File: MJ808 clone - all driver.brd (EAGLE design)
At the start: 22 x 22 mm, 35 parts, among them IC1 ATTINY4313-MMH, IC2 PRQV8.00CR1510Y00L, IC3 LP38693SD-5.0/NOPB, IC4 LP38693SD-5.0/NOPB, IC5 MCP2515, IC6 MCP2561-2, IC7 MAX16820, Q1 PMV213SN,215, SW1 TL3305-844809

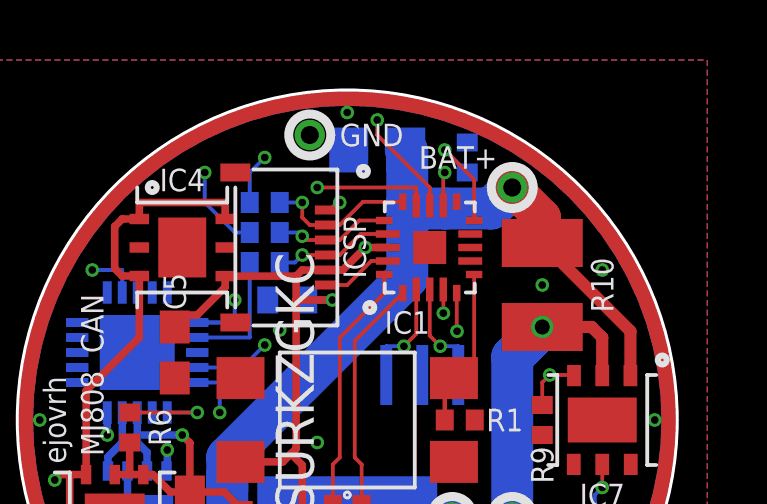
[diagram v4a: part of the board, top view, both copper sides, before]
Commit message: - rerouted standby pin, updated gerbers
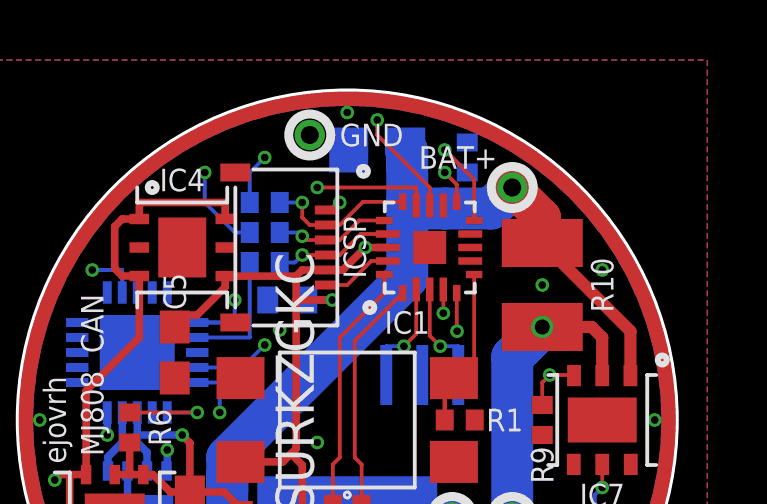
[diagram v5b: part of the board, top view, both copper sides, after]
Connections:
- net N$3: now also IC1.PB2; no longer IC1.PB1
- net STBY: now also IC1.PB1; no longer IC1.PB2
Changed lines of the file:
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@@
 <layers>
 <layer number="1" name="Top" color="4" fill="1" visible="yes" active="yes"/>
-<layer number="2" name="Route2" color="1" fill="3" visible="yes" active="yes"/>
+<layer number="2" name="Route2" color="1" fill="3" visible="no" active="yes"/>
 <layer number="3" name="Route3" color="4" fill="3" visible="no" active="no"/>
 <layer number="4" name="Route4" color="1" fill="4" visible="no" active="no"/>
@@
 <layer number="13" name="Route13" color="4" fill="5" visible="no" active="no"/>
 <layer number="14" name="Route14" color="1" fill="6" visible="no" active="no"/>
-<layer number="15" name="Route15" color="4" fill="6" visible="yes" active="yes"/>
+<layer number="15" name="Route15" color="4" fill="6" visible="no" active="yes"/>
 <layer number="16" name="Bottom" color="1" fill="1" visible="yes" active="yes"/>
 <layer number="17" name="Pads" color="2" fill="1" visible="yes" active="yes"/>
@@
 <contactref element="IC6" pad="STBY"/>
 <contactref element="R11" pad="2"/>
-<contactref element="IC1" pad="PB2"/>
 <via x="3.25" y="8.25" extent="1-16" drill="0.254"/>
-<wire x1="3.25" y1="8.25" x2="3.25" y2="4.5" width="0.254" layer="15"/>
-<wire x1="3.25" y1="4.5" x2="-5.290875" y2="-4.040875" width="0.254" layer="15"/>
+<wire x1="3.25" y1="8.25" x2="3.25" y2="5.25" width="0.254" layer="15"/>
 <wire x1="-7.975" y1="-4.8" x2="-7.975" y2="-5.975" width="0.127" layer="16"/>
 <via x="-7.375" y="-6.875" extent="1-16" drill="0.254"/>
@@
 <wire x1="-7.975" y1="-4.8" x2="-7.975" y2="-6.275" width="0.127" layer="16"/>
 <wire x1="-7.975" y1="-6.275" x2="-7.375" y2="-6.875" width="0.127" layer="16"/>
-<wire x1="-5.290875" y1="-5.25" x2="-5.290875" y2="-4.040875" width="0.254" layer="15"/>
+<wire x1="-5.290875" y1="-5.25" x2="-5.290875" y2="-3.290875" width="0.254" layer="15"/>
 <wire x1="-7.375" y1="-6.875" x2="-6.915875" y2="-6.875" width="0.254" layer="15"/>
 <wire x1="-6.915875" y1="-6.875" x2="-5.290875" y2="-5.25" width="0.254" layer="15"/>
@@
 <wire x1="-3.5" y1="-4" x2="-3.5" y2="-4.207" width="0.127" layer="1"/>
 <wire x1="-3.5" y1="-4.207" x2="-4.5" y2="-5.207" width="0.127" layer="1"/>
-<wire x1="3.2" y1="7.15" x2="3.2" y2="8.2" width="0.127" layer="1"/>
-<wire x1="3.2" y1="8.2" x2="3.25" y2="8.25" width="0.127" layer="1"/>
+<contactref element="IC1" pad="PB1"/>
+<wire x1="3.65" y1="7.27" x2="3.65" y2="7.85" width="0.127" layer="1"/>
+<wire x1="3.65" y1="7.85" x2="3.25" y2="8.25" width="0.127" layer="1"/>
+<wire x1="-5.290875" y1="-3.290875" x2="3.25" y2="5.25" width="0.254" layer="15"/>
 </signal>
 <signal name="ICSP_MOSI" class="2">
@@
 <contactref element="IC1" pad="PD6"/>
 </signal>
-<signal name="N$3">
-<contactref element="IC1" pad="PB1"/>
-</signal>
 <signal name="N$2">
 <contactref element="IC1" pad="PD5"/>
 </signal>
+<signal name="N$3">
+<contactref element="IC1" pad="PB2"/>
+</signal>
 </signals>

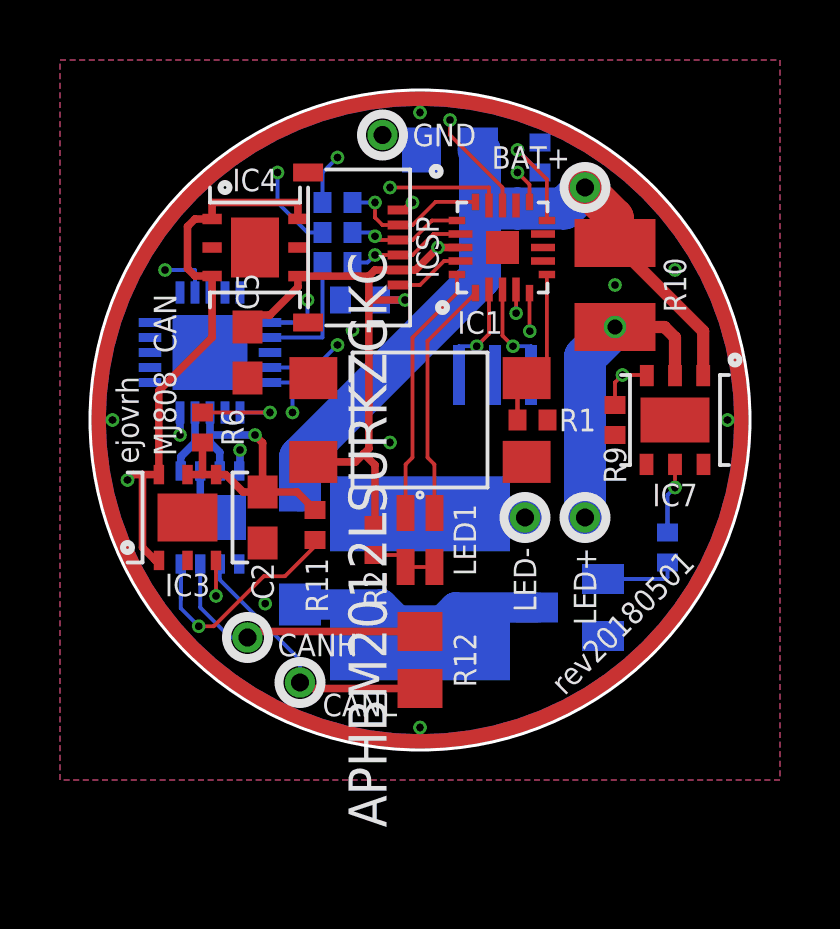
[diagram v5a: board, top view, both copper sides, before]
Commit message: - fine-tuned POC and final board, they are in sync, ERC & DRC check out, updated gerbers, cleaned up BOM
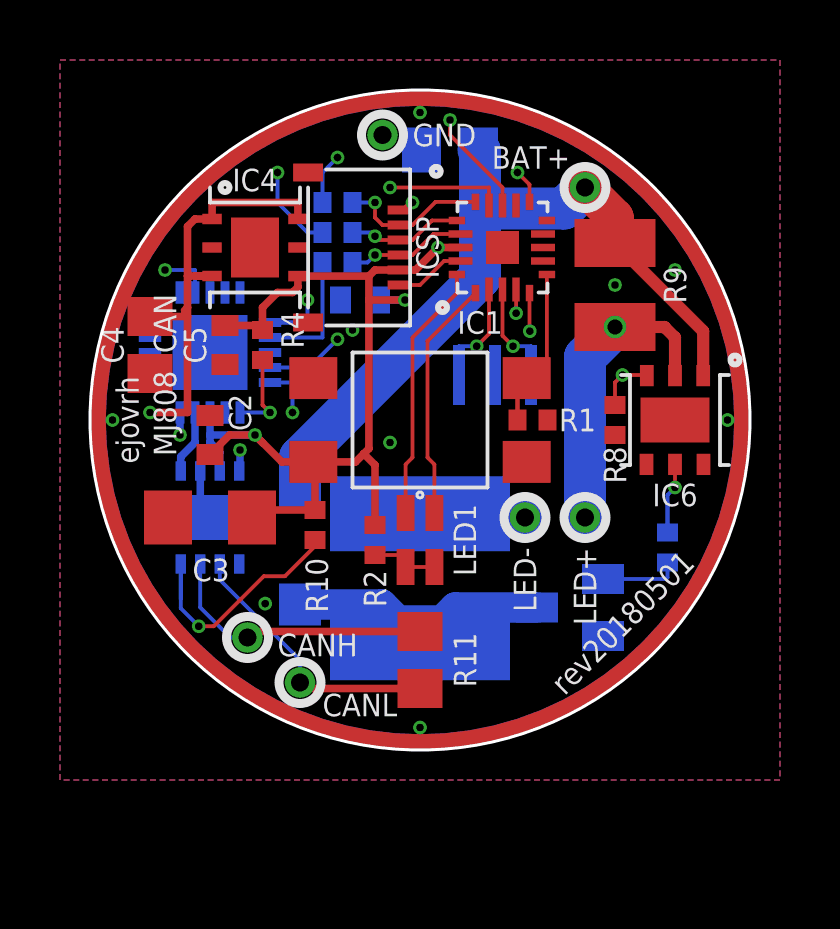
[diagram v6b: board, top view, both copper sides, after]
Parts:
- removed IC7: MAX16820, MAX16820 LED Driver, constant current:TDFN-6-EP
- removed R12: 120, rcl:R0805
- added C3: 100μF, rcl:C1206
- added C6: 47μF, rcl:C0805
- C1: value 0.1μF -> 1μF
- C2, C5: value 22μF -> 1μF; device rcl:C0603 -> rcl:C0402
- C4: value 47μF / 15V+ -> 47μF
- IC2: value PRQV8.00CR1510Y00L -> PRQV8.00CR1510Y00L
- IC3: value LP38693SD-5.0/NOPB -> MCP2515; device LP38693 5V LDO:WSON6 -> MCP2515-I-ML - Standalonce CAN Controller with SPI Interface:QFN20
- IC5: value MCP2515 -> MCP2561-2; device MCP2515-I-ML - Standalonce CAN Controller with SPI Interface:QFN20 -> MCP2561-2 - High-Speed CAN Transceiver:DFN10
- IC6: value MCP2561-2 -> MAX16820; device MCP2561-2 - High-Speed CAN Transceiver:DFN10 -> MAX16820 LED Driver, constant current:TDFN-6-EP
- R10: value 0.15 / 1W -> 10k; device rcl:R1210 -> rcl:R0402
- R11: value 10k -> 120; device rcl:R0402 -> rcl:R0805
- R3, R6: value 10k -> 330
- R4, R7: value 330 -> 10k
- R9: value 10k -> 0.15 / 1W; device rcl:R0402 -> rcl:R1210
- moved IC6 15.8 mm to (8.50, 0.00), flipped to the top, turned to 270 degrees
- moved R7 15.2 mm to (8.25, -4.25), turned to 270 degrees
- moved R10 12.8 mm to (-3.50, -3.50), turned to 270 degrees
- moved C4 11.9 mm to (-9.00, 2.50), flipped to the top, turned to 90 degrees
- moved R6 7.91 mm to (-2.75, 6.25), flipped to the bottom, turned to 180 degrees
- moved R3 7.60 mm to (-2.75, 5.25), turned to 180 degrees
- moved R11 5.70 mm to (0.00, -8.00), turned to 90 degrees
- moved IC3 5.55 mm to (-7.00, 2.25), flipped to the bottom, turned to 180 degrees
- moved IC5 5.50 mm to (-7.00, -3.25)
- moved R8 4.60 mm to (6.50, 0.00), flipped to the top
- moved R9 4.50 mm to (6.50, 4.50), turned to 90 degrees
- moved R4 3.72 mm to (-5.25, 2.50), flipped to the top, turned to 270 degrees
- moved C2 3.26 mm to (-7.00, -0.50), turned to 90 degrees
- moved C5 0.79 mm to (-6.50, 2.50), turned to 270 degrees
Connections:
- removed net 5V0_CAN: C2.1, IC3.4-OUT, IC3.5-SNS, IC5.VDD, IC6.VDD, R11.1, R6.1
- removed net 5V0_μC: C1.1, C5.2, IC1.VCC, IC4.4-OUT, ICSP.5, R2.2, SW1.1, SW1.2
- removed net EN: IC1.PB0, IC3.3-EN, R3.2
- new net 5V0: C1.1, C2.1, C3.2, C5.1, IC1.VCC, IC3.VDD, IC4.4-OUT, IC5.VDD, ICSP.5, R10.1, R2.2, R4.1, SW1.1, SW1.2
- new net N$4: IC1.PB0
- net BAT+: now also C4.2, C6.1, IC6.IN, R9.2; no longer C4.1, IC3.1-IN, IC3.6-IN, IC7.IN, R10.2
- net CANH: now also IC5.CANH, R11.2; no longer IC6.CANH, R12.2
- net CANL: now also IC5.CANL, R11.1; no longer IC6.CANL, R12.1
- net CLOCKOUT: now also IC3.OSC1; no longer IC5.OSC1
- net DIM_FRONT: now also IC6.DIM, R8.1; no longer IC7.DIM, R9.1
- net DIM_FRONT_GATE: now also IC6.DRV, R7.1; no longer IC7.DRV, R8.1
- net GATE: now also R7.2; no longer R8.2
- net GND: now also C3.1, C4.1, C5.2, C6.2, IC3.GND, IC3.GND6, IC5.VSS, IC6.GND1, R8.2; no longer C4.2, C5.1, IC3.2-GND, IC3.GND1, IC5.GND6, IC6.VSS, IC7.GND, IC7.GND1, R3.1, R9.2
- net ICSP_MISO: now also R6.2; no longer R7.2
- net ICSP_SCK: now also R3.2; no longer R4.2
- net INT: now also IC3.!INT!; no longer IC5.!INT!
- net LED_AN: now also IC6.CSN, R9.1; no longer IC7.CSN, R10.1
- net RXCAN: now also IC3.RXCAN, IC5.RXD; no longer IC5.RXCAN, IC6.RXD
- net SPI_MISO: now also IC3.SO, R6.1; no longer IC5.SO, R7.1
- net SPI_MOSI: now also IC3.SI; no longer IC5.SI
- net SPI_SCK: now also IC3.SCK, R3.1; no longer IC5.SCK, R4.1
- net SPI_SS: now also IC3.!CS!, R4.2; no longer IC5.!CS!, R6.2
- net STBY: now also IC5.STBY, R10.2; no longer IC6.STBY, R11.2
- net TXCAN: now also IC3.TXCAN, IC5.TXD; no longer IC5.TXCAN, IC6.TXD
- net VCC: now also IC6.VCC; no longer IC7.VCC
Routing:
- net 5V0: track 0.00 -> 34.1 mm, vias 0 -> 3
- net EN: track 24.0 -> 0.00 mm, vias 2 -> 0
- net 5V0_μC: track 20.8 -> 0.00 mm, vias 2 -> 0
- net 5V0_CAN: track 11.9 -> 0.00 mm, vias 1 -> 0
- net BAT+: track 68.2 -> 62.9 mm
